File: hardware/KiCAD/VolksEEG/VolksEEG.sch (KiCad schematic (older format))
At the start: 0 parts

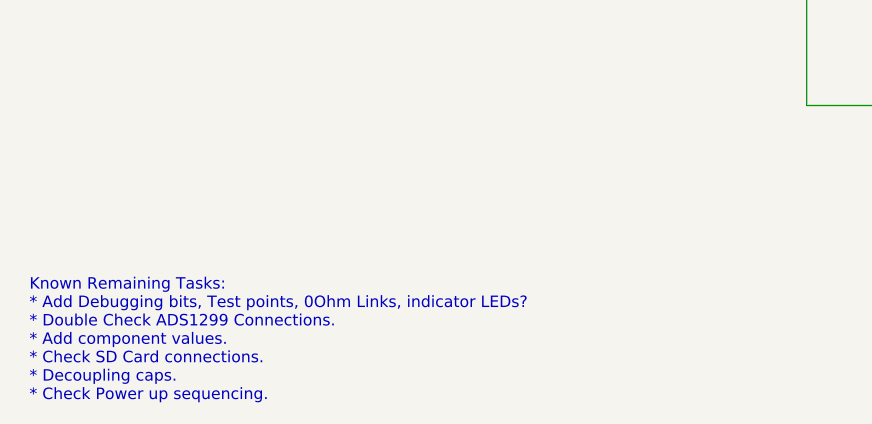
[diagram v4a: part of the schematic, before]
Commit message: Added debugging bits to the NRF schematic sheet.
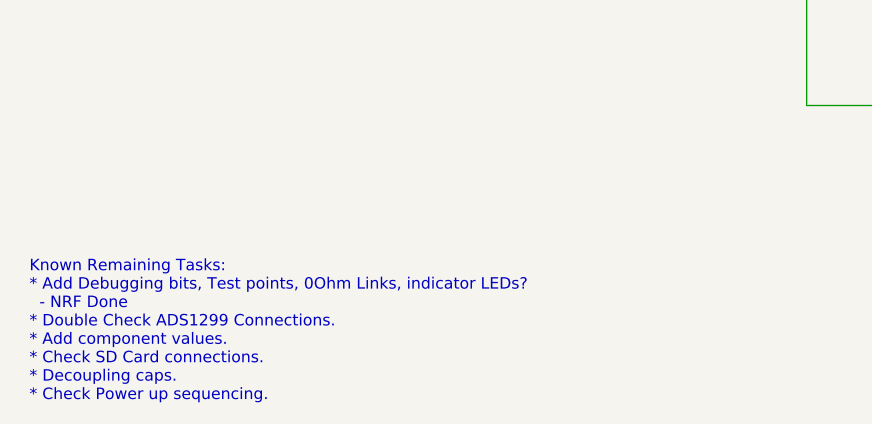
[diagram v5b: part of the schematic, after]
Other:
- note added: "Known Remaining Tasks:\n* Add Debugging bits, Test points, 0Ohm Links, indicator LEDs? \n - NRF Done\n* Double Check ADS1299 Connections.\n* Add component values.\n* Check SD Card connections.\n* Decoupling caps.\n* Check Power up sequencing."
- note removed: "Known Remaining Tasks:\n* Add Debugging bits, Test points, 0Ohm Links, indicator LEDs? \n* Double Check ADS1299 Connections.\n* Add component values.\n* Check SD Card connections.\n* Decoupling caps.\n* Check Power up sequencing."
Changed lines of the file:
@@
 	7650 3850 8150 3850
 Text Notes 1550 5550 0    50   ~ 0
-Known Remaining Tasks:\n* Add Debugging bits, Test points, 0Ohm Links, indicator LEDs? \n* Double Check ADS1299 Connections.\n* Add component values.\n* Check SD Card connections.\n* Decoupling caps.\n* Check Power up sequencing.
+Known Remaining Tasks:\n* Add Debugging bits, Test points, 0Ohm Links, indicator LEDs? \n  - NRF Done\n* Double Check ADS1299 Connections.\n* Add component values.\n* Check SD Card connections.\n* Decoupling caps.\n* Check Power up sequencing.
 Wire Wire Line
 	6600 3400 6250 3400

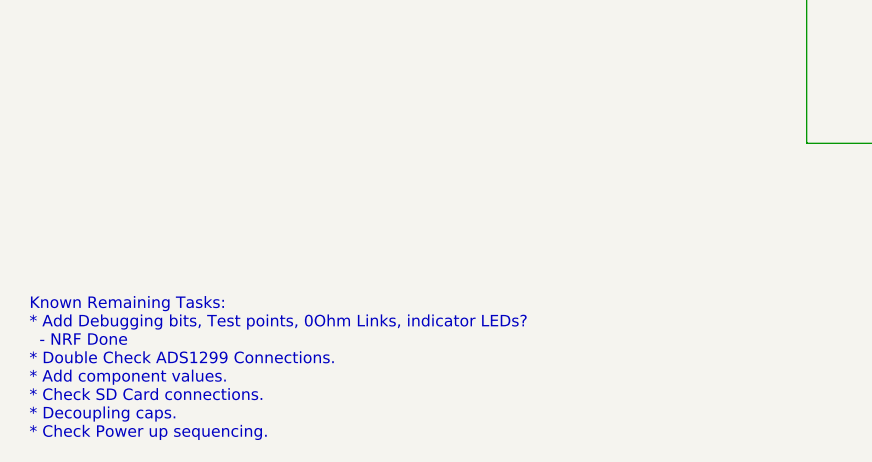
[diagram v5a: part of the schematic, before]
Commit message: Added debugging bits to more schematic sheets.
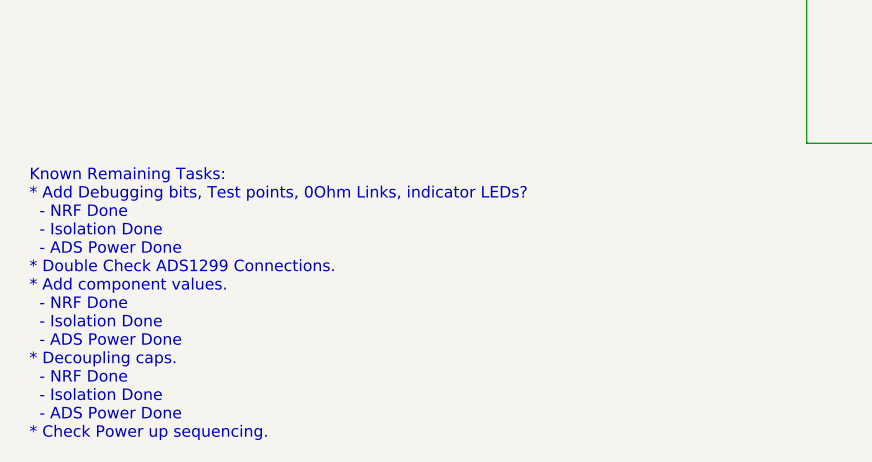
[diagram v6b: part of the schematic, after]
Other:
- note added: "Known Remaining Tasks:\n* Add Debugging bits, Test points, 0Ohm Links, indicator LEDs? \n - NRF Done\n - Isolation Done\n - ADS Power Done\n* Double Check ADS1299 Connections.\n* Add component values.\n - NRF Done\n - Isolation Done\n - ADS Power Done\n* Decoupling caps.\n - NRF Done\n - Isolation Done\n - ADS Power Done\n* Check Power up sequencing."
- note removed: "Known Remaining Tasks:\n* Add Debugging bits, Test points, 0Ohm Links, indicator LEDs? \n - NRF Done\n* Double Check ADS1299 Connections.\n* Add component values.\n* Check SD Card connections.\n* Decoupling caps.\n* Check Power up sequencing."
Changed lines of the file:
@@
 	7650 3850 8150 3850
 Text Notes 1550 5550 0    50   ~ 0
-Known Remaining Tasks:\n* Add Debugging bits, Test points, 0Ohm Links, indicator LEDs? \n  - NRF Done\n* Double Check ADS1299 Connections.\n* Add component values.\n* Check SD Card connections.\n* Decoupling caps.\n* Check Power up sequencing.
+Known Remaining Tasks:\n* Add Debugging bits, Test points, 0Ohm Links, indicator LEDs? \n  - NRF Done\n  - Isolation Done\n  - ADS Power Done\n* Double Check ADS1299 Connections.\n* Add component values.\n  - NRF Done\n  - Isolation Done\n  - ADS Power Done\n* Decoupling caps.\n  - NRF Done\n  - Isolation Done\n  - ADS Power Done\n* Check Power up sequencing.
 Wire Wire Line
 	6600 3400 6250 3400

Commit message: finished off tasks list.
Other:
- note removed: "Known Remaining Tasks:\n* Add Debugging bits, Test points, 0Ohm Links, indicator LEDs? \n - NRF Done\n - Isolation Done\n - ADS Power Done\n* Double Check ADS1299 Connections.\n* Add component values.\n - NRF Done\n - Isolation Done\n - ADS Power Done\n* Decoupling caps.\n - NRF Done\n - Isolation Done\n - ADS Power Done\n* Check Power up sequencing."
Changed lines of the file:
@@
 Wire Wire Line
 	4800 2100 6400 2100
-Connection ~ 6400 3250
-Wire Wire Line
-	6400 3250 6600 3250
 Wire Wire Line
 	5050 3150 5050 3250
 Wire Wire Line
 	5050 3250 5250 3250
-Wire Wire Line
-	6400 4250 4950 4250
-Wire Wire Line
-	4950 4250 4950 3400
-Connection ~ 4950 3400
 $Sheet
 S 8150 1750 800  2350
@@
 Wire Wire Line
 	7650 3850 8150 3850
-Text Notes 1550 5550 0    50   ~ 0
-Known Remaining Tasks:\n* Add Debugging bits, Test points, 0Ohm Links, indicator LEDs? \n  - NRF Done\n  - Isolation Done\n  - ADS Power Done\n* Double Check ADS1299 Connections.\n* Add component values.\n  - NRF Done\n  - Isolation Done\n  - ADS Power Done\n* Decoupling caps.\n  - NRF Done\n  - Isolation Done\n  - ADS Power Done\n* Check Power up sequencing.
 Wire Wire Line
 	6600 3400 6250 3400
@@
 F6 "+5V" I L 5250 3250 50
 F7 "GNDA" O R 6250 3700 50
+F8 "+3V3A" O R 6250 3850 50
 $EndSheet
-Wire Wire Line
-	6400 3850 6400 4250
-Wire Wire Line
-	6600 3850 6400 3850
 $Sheet
 S 6600 1750 1050 2350
@@
 F14 "AIN4" I R 7650 2700 50
 F15 "ADS_nDRDY" O L 6600 3000 50
-F16 "+3V3" I L 6600 3250 50
+F16 "+3V3A" I L 6600 3850 50
 F17 "+2V5" I L 6600 3400 50
 F18 "-2V5" I L 6600 3550 50
-F19 "GNDD" I L 6600 3850 50
-F20 "REF" I R 7650 3550 50
-F21 "BIAS_OUT" O R 7650 3700 50
-F22 "BIAS_INV" O R 7650 3850 50
-F23 "GNDA" I L 6600 3700 50
+F19 "REF" I R 7650 3550 50
+F20 "BIAS_OUT" O R 7650 3700 50
+F21 "BIAS_INV" O R 7650 3850 50
+F22 "GNDA" I L 6600 3700 50
 $EndSheet
+Wire Wire Line
+	6250 3850 6600 3850
 $EndSCHEMATC

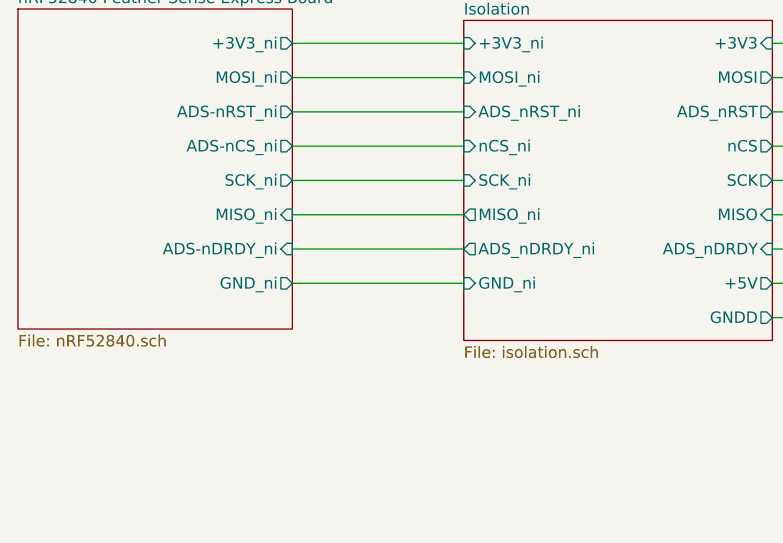
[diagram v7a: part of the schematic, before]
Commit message: Annotated schematic and cleared ERC errors.
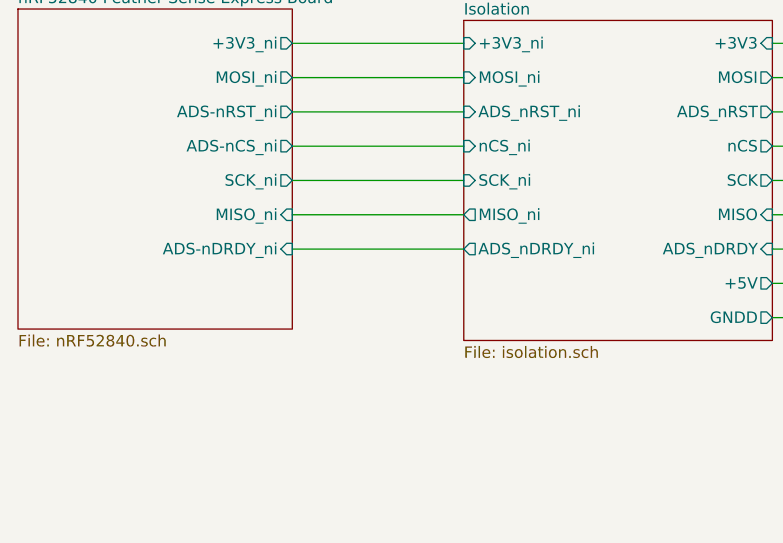
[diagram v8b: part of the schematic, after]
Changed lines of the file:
@@
 F7 "ADS-nDRDY_ni" I R 2700 3000 50
 F8 "+3V3_ni" O R 2700 2100 50
-F9 "GND_ni" O R 2700 3150 50
 $EndSheet
 Wire Wire Line
@@
 Wire Wire Line
 	2700 2100 3450 2100
-Wire Wire Line
-	2700 3150 3450 3150
-$Sheet
-S 3450 2000 1350 1400
-U 61731DC5
-F0 "Isolation" 50
-F1 "isolation.sch" 50
-F2 "+3V3_ni" I L 3450 2100 50
-F3 "GND_ni" I L 3450 3150 50
-F4 "+3V3" I R 4800 2100 50
-F5 "GNDD" O R 4800 3300 50
-F6 "MOSI" O R 4800 2250 50
-F7 "ADS_nRST" O R 4800 2400 50
-F8 "nCS" O R 4800 2550 50
-F9 "SCK" O R 4800 2700 50
-F10 "MISO" I R 4800 2850 50
-F11 "ADS_nDRDY" I R 4800 3000 50
-F12 "MOSI_ni" I L 3450 2250 50
-F13 "ADS_nRST_ni" I L 3450 2400 50
-F14 "nCS_ni" I L 3450 2550 50
-F15 "SCK_ni" I L 3450 2700 50
-F16 "MISO_ni" O L 3450 2850 50
-F17 "ADS_nDRDY_ni" O L 3450 3000 50
-F18 "+5V" O R 4800 3150 50
-$EndSheet
 Wire Wire Line
 	4800 3150 5050 3150
@@
 Wire Wire Line
 	6250 3850 6600 3850
+$Sheet
+S 3450 2000 1350 1400
+U 61731DC5
+F0 "Isolation" 50
+F1 "isolation.sch" 50
+F2 "+3V3_ni" I L 3450 2100 50
+F3 "+3V3" I R 4800 2100 50
+F4 "GNDD" O R 4800 3300 50
+F5 "MOSI" O R 4800 2250 50
+F6 "ADS_nRST" O R 4800 2400 50
+F7 "nCS" O R 4800 2550 50
+F8 "SCK" O R 4800 2700 50
+F9 "MISO" I R 4800 2850 50
+F10 "ADS_nDRDY" I R 4800 3000 50
+F11 "MOSI_ni" I L 3450 2250 50
+F12 "ADS_nRST_ni" I L 3450 2400 50
+F13 "nCS_ni" I L 3450 2550 50
+F14 "SCK_ni" I L 3450 2700 50
+F15 "MISO_ni" O L 3450 2850 50
+F16 "ADS_nDRDY_ni" O L 3450 3000 50
+F17 "+5V" O R 4800 3150 50
+$EndSheet
 $EndSCHEMATC
